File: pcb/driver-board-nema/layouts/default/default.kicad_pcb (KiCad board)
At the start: 2 copper layers, 62 x 76 mm, 34 parts

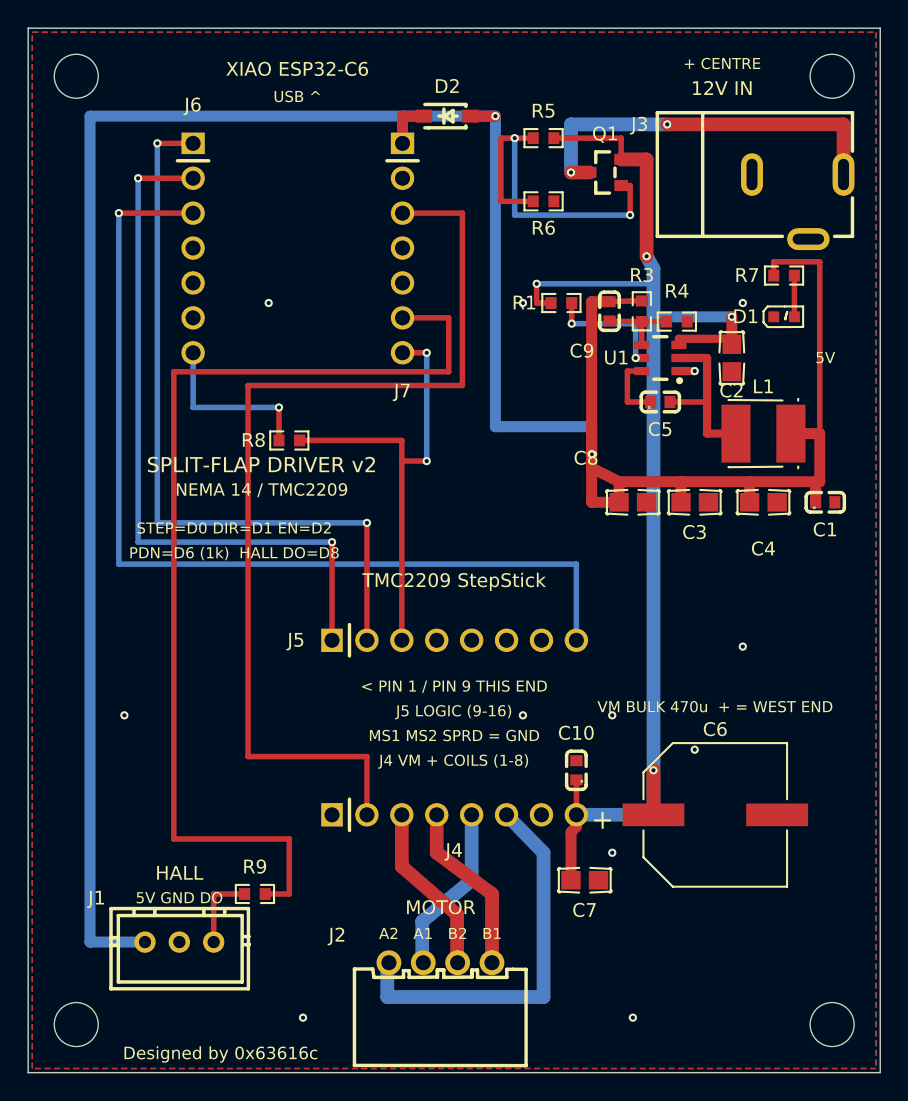
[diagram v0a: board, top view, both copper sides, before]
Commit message: chore(pcb): regenerate layouts, fab packages and renders
Both boards: 0 DRC errors, 0 warnings on v1 (four spurious silk_overlap
warnings remain on v2's C8 -- re-confirmed spurious, they are byte-identical
with the reference field moved ~24mm away), 0 unconnected pads, 0 footprint
errors, courtyard checks active and passing, and verify_fab clean.

Claude-Session: https://claude.ai/code/session_01UQXFTEy3DeBEx85CfiBq9q
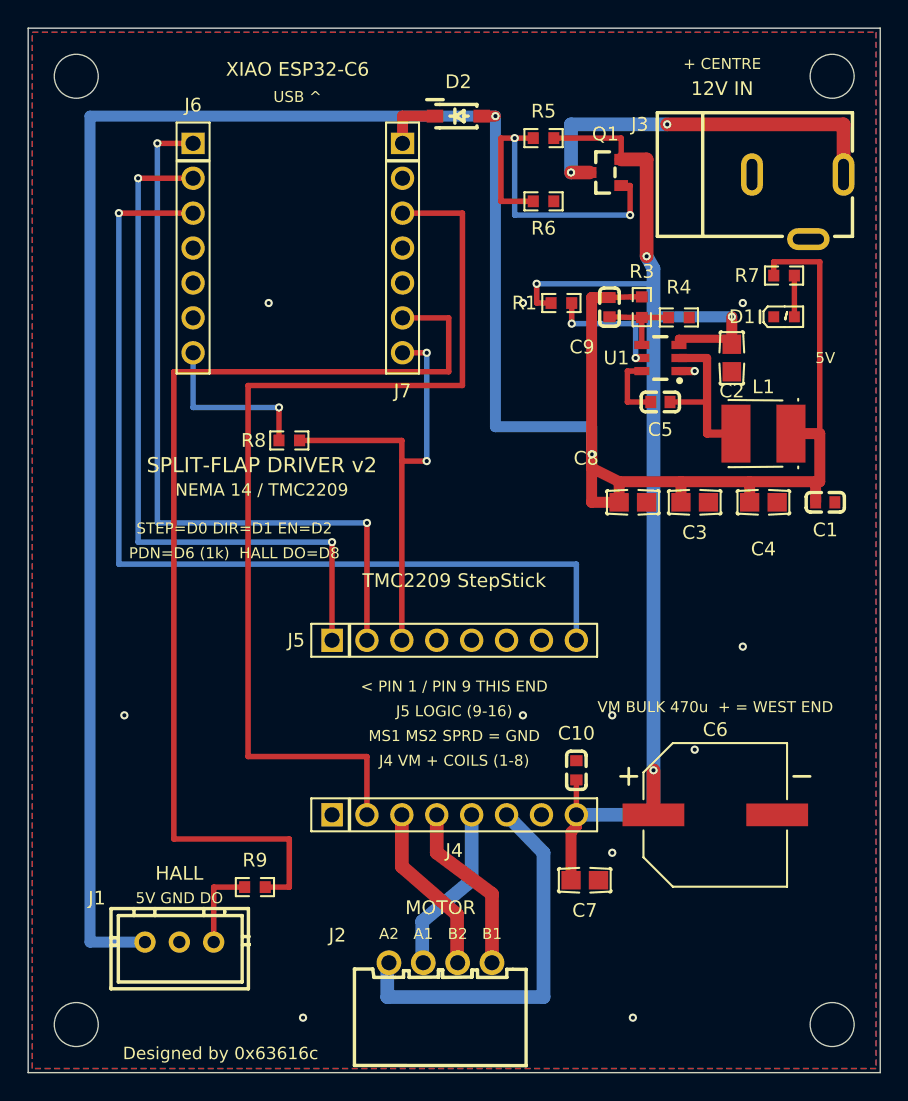
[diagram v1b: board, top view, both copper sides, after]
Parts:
- moved D2 0.80 mm to (31.3, 6.40)
- moved R9 0.50 mm to (16.5, 62.5)
- moved R4 0.34 mm to (47.4, 21.1)
- moved C9 0.30 mm to (42.3, 20.3)
- moved R3 0.30 mm to (44.6, 20.3)
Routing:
- net p5v_xiao: track 3.54 -> 4.34 mm
- net hall_raw: track 5.75 -> 6.25 mm
- net hall_do: track 75.4 -> 74.9 mm
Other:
- board text removed: "+"
